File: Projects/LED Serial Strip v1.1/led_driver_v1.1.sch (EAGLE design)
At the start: 97 parts, among them U1 TLC5947DAP, U2 TLC5947DAP, U3 74LS595D, U4 UDN2982SLW, U5 74LS595D, U6 UDN2982SLW, U7 ARDUINO_R3_SHIELD

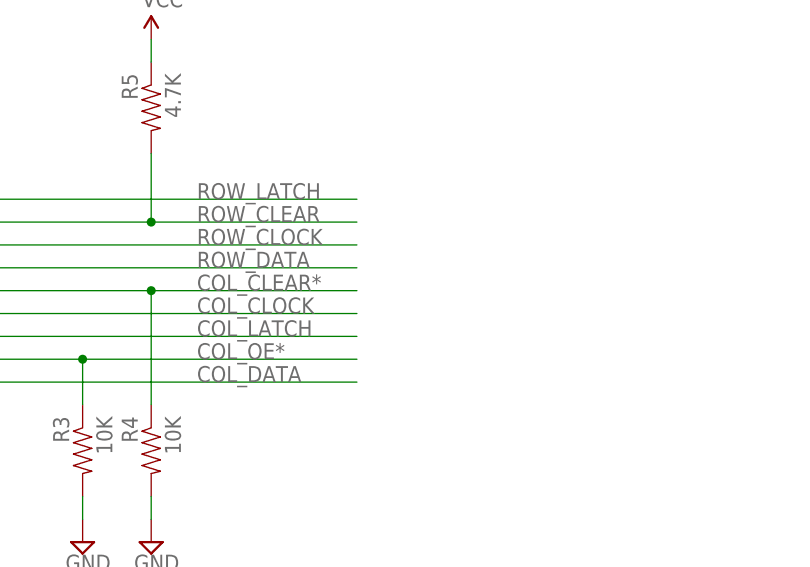
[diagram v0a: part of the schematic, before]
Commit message: 
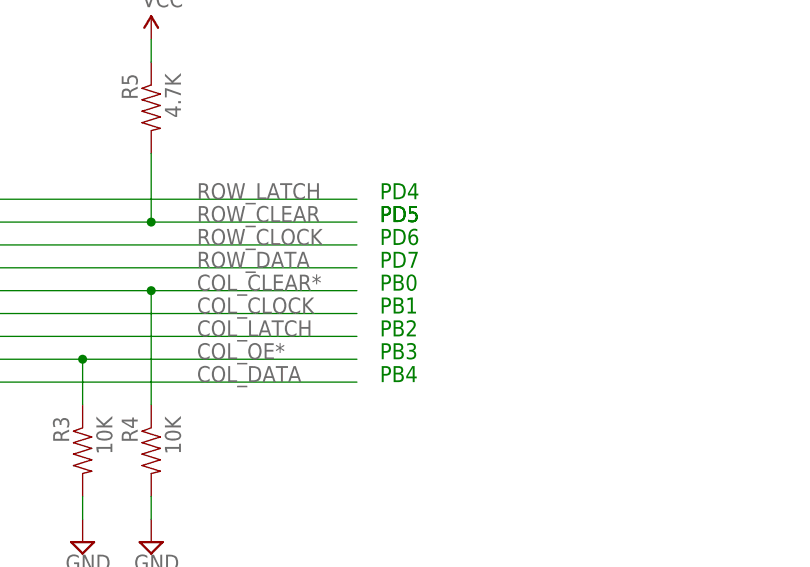
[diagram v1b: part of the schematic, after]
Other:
- note added: "PB0"
- note added: "PB1"
- note added: "PB2"
- note added: "PB3"
- note added: "PB4"
- note added: "PD4"
- note added: "PD5"
- note added: "PD6"
- note added: "PD7"
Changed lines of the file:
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@@
 <?xml version="1.0" encoding="utf-8"?>
 <!DOCTYPE eagle SYSTEM "eagle.dtd">
-<eagle version="6.5.0">
+<eagle version="7.1.0">
 <drawing>
 <settings>
@@
 <wire x1="302.26" y1="35.56" x2="302.26" y2="68.58" width="0.4064" layer="97" style="shortdash"/>
 <text x="304.8" y="66.04" size="1.778" layer="97" font="vector" ratio="15" align="top-left">Decoupling</text>
+<text x="157.48" y="71.12" size="1.778" layer="91">PD4</text>
+<text x="157.48" y="68.58" size="1.778" layer="91">PD5</text>
+<text x="157.48" y="68.58" size="1.778" layer="91">PD5</text>
+<text x="157.48" y="66.04" size="1.778" layer="91">PD6</text>
+<text x="157.48" y="63.5" size="1.778" layer="91">PD7</text>
+<text x="157.48" y="60.96" size="1.778" layer="91">PB0</text>
+<text x="157.48" y="58.42" size="1.778" layer="91">PB1</text>
+<text x="157.48" y="55.88" size="1.778" layer="91">PB2</text>
+<text x="157.48" y="53.34" size="1.778" layer="91">PB3</text>
+<text x="157.48" y="50.8" size="1.778" layer="91">PB4</text>
 </plain>
 <instances>
